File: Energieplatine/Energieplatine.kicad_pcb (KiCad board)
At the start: 2 copper layers, 13 parts, among them J1 USB_C_Receptacle_PowerOnly_6P, J2 Conn_01x02_Pin, U1 4027, U2 TL072, U3 LM2576HVT-ADJ

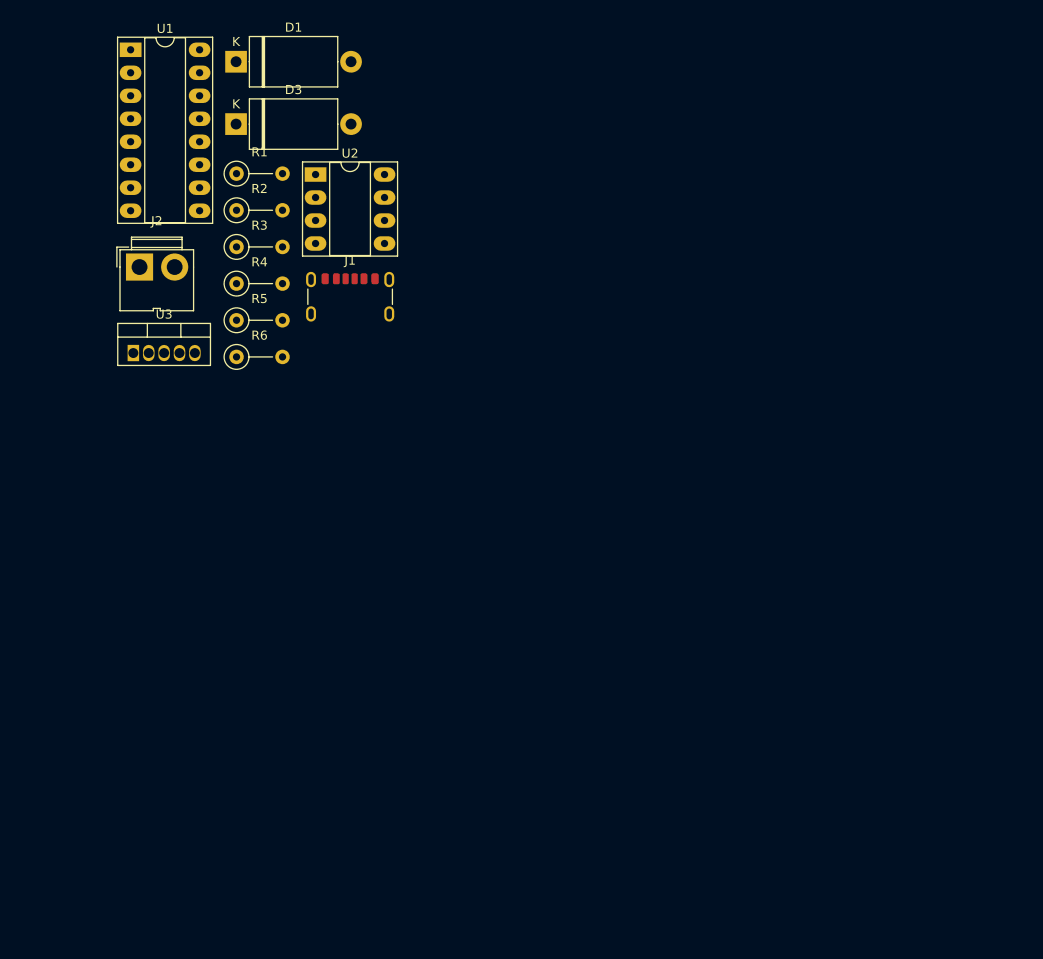
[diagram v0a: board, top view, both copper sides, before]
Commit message: Layout is has no DRC errors.
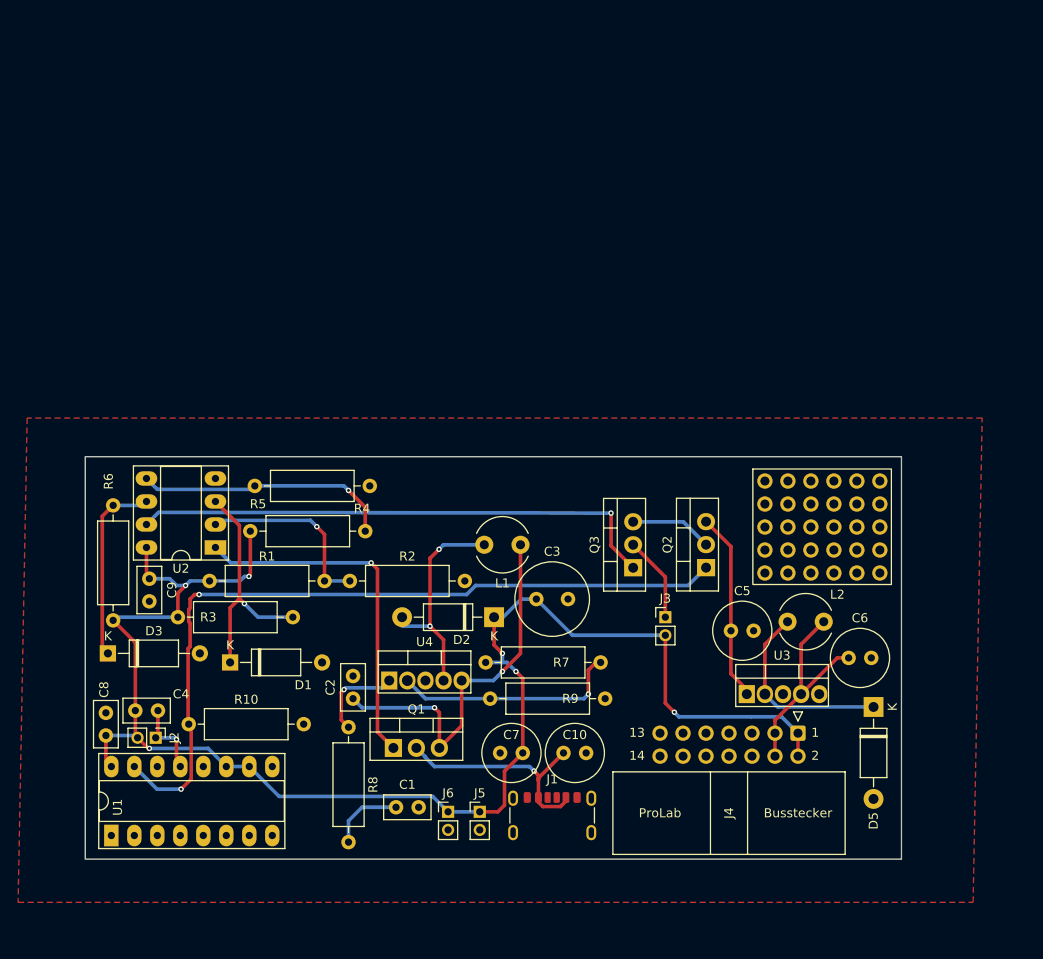
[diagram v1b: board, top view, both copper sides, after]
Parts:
- added C1: 330n, Capacitor_THT:C_Disc_D5.0mm_W2.5mm_P2.50mm, F.Cu at (128.8, 149.5)
- added C10: 100u, Capacitor_THT:C_Radial_D6.3mm_H11.0mm_P2.50mm, F.Cu at (147.2, 143.5)
- added C2: 100n, Capacitor_THT:C_Disc_D5.0mm_W2.5mm_P2.50mm, F.Cu at (124.0, 137.5)
- added C3: 470u, Capacitor_THT:C_Radial_D8.0mm_H11.5mm_P3.50mm, F.Cu at (144.2, 126.5)
- added C4: 100n, Capacitor_THT:C_Disc_D5.0mm_W2.5mm_P2.50mm, F.Cu at (102.5, 138.8)
- added C5: 100u, Capacitor_THT:C_Radial_D6.3mm_H11.0mm_P2.50mm, F.Cu at (165.8, 130.0)
- added C6: 100u, Capacitor_THT:C_Radial_D6.3mm_H11.0mm_P2.50mm, F.Cu at (178.8, 133.0)
- added C7: 100u, Capacitor_THT:C_Radial_D6.3mm_H11.0mm_P2.50mm, F.Cu at (140.2, 143.5)
- added C8: 100n, Capacitor_THT:C_Disc_D5.0mm_W2.5mm_P2.50mm, F.Cu at (96.7, 141.6)
- added C9: 100n, Capacitor_THT:C_Disc_D5.0mm_W2.5mm_P2.50mm, F.Cu at (101.5, 124.2)
- added D2: 1N5817, Diode_THT:D_DO-41_SOD81_P10.16mm_Horizontal, F.Cu at (139.6, 128.5)
- added D5: 1N5822, Diode_THT:D_DO-41_SOD81_P10.16mm_Horizontal, F.Cu at (181.5, 138.4)
- added J3: Conn_01x02_Pin, Connector_PinHeader_2.00mm:PinHeader_1x02_P2.00mm_Vertical, F.Cu at (158.5, 128.5)
- added J4: Conn_02x07_Odd_Even, Projektlabor:Prolab_Busstecker, F.Cu at (165.5, 142.5)
- added J5: Conn_01x02_Pin, Connector_PinHeader_2.00mm:PinHeader_1x02_P2.00mm_Vertical, F.Cu at (138.0, 150.0)
- added J6: Conn_01x02_Pin, Connector_PinHeader_2.00mm:PinHeader_1x02_P2.00mm_Vertical, F.Cu at (134.5, 150.0)
- added L1: 100u, Inductor_THT:L_Radial_D6.0mm_P4.00mm, F.Cu at (142.5, 120.5)
- added L2: 100u, Inductor_THT:L_Radial_D6.0mm_P4.00mm, F.Cu at (172.0, 129.0)
- added Q1: IRF9540N, Package_TO_SOT_THT:TO-220-3_Vertical, F.Cu at (128.5, 142.9)
- added Q2: IRF9540N, Package_TO_SOT_THT:TO-220-3_Vertical, F.Cu at (163.0, 123.0)
- added Q3: IRF540N, Package_TO_SOT_THT:TO-220-3_Vertical, F.Cu at (154.9, 123.0)
- added R10: 1k, Resistor_THT:R_Axial_DIN0309_L9.0mm_D3.2mm_P12.70mm_Horizontal, F.Cu at (105.8, 140.3)
- added R7: 410k, Resistor_THT:R_Axial_DIN0309_L9.0mm_D3.2mm_P12.70mm_Horizontal, F.Cu at (138.7, 133.5)
- added R8: 2.2k, Resistor_THT:R_Axial_DIN0309_L9.0mm_D3.2mm_P12.70mm_Horizontal, F.Cu at (123.5, 140.7)
- added R9: 41k, Resistor_THT:R_Axial_DIN0309_L9.0mm_D3.2mm_P12.70mm_Horizontal, F.Cu at (139.2, 137.5)
- added REF**: Panikraster_05x05, Panikraster_v2:Panikraster_05x05, F.Cu at (169.5, 113.5)
- added U4: LM2577T-ADJ, Projektlabor:TO-220-5_Vertical_Brolab, F.Cu at (128.5, 135.5)
- D1, D3: footprint Diode_THT:D_DO-27_P12.70mm_Horizontal -> Diode_THT:D_A-405_P10.16mm_Horizontal
- J2: footprint Connector:JWT_A3963_1x02_P3.96mm_Vertical -> Connector_PinHeader_2.00mm:PinHeader_1x02_P2.00mm_Vertical
- R1, R2, R3, R4, R5, R6: footprint Resistor_THT:R_Axial_DIN0207_L6.3mm_D2.5mm_P5.08mm_Vertical -> Resistor_THT:R_Axial_DIN0309_L9.0mm_D3.2mm_P12.70mm_Horizontal
- U3: footprint Package_TO_SOT_THT:TO-220-5_Vertical -> Projektlabor:TO-220-5_Vertical_Brolab
- moved U1 86.8 mm to (97.3, 152.6), turned to 90 degrees
- moved U3 78.0 mm to (168.0, 137.0)
- moved D1 66.4 mm to (110.4, 133.5)
- moved J1 61.5 mm to (146.0, 151.5)
- moved D3 60.2 mm to (96.9, 132.5)
- moved J2 52.0 mm to (102.2, 141.8), turned to -90 degrees
- moved R1 45.1 mm to (108.2, 124.5)
- moved R2 42.8 mm to (123.7, 124.5)
- moved U2 42.7 mm to (108.8, 120.8), turned to 180 degrees
- moved R3 41.4 mm to (104.7, 128.5)
- moved R6 32.1 mm to (97.5, 128.8), turned to 90 degrees
- moved R4 27.4 mm to (112.7, 119.0)
- moved R5 18.4 mm to (113.2, 114.0)
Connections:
- U2 pad 7: unconnected-(U2-Pad7) -> undervoltage_logic
- U3 pad 1: unconnected-(U3-VIN-Pad1) -> Net-(Q2-S)
- U3 pad 2: unconnected-(U3-OUT-Pad2) -> Net-(D5-K)
- U3 pad 3: unconnected-(U3-GND-Pad3) -> GND
- U3 pad 4: unconnected-(U3-FB-Pad4) -> Power_5V
- U3 pad 5: unconnected-(U3-~{ON}/OFF-Pad5) -> GND
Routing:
- net Bat+_12V: track 0.00 -> 169.6 mm, vias 0 -> 6
- net FF_out: track 0.00 -> 86.5 mm, vias 0 -> 2
- net undervoltage_logic: track 0.00 -> 59.0 mm, vias 0 -> 1
- net Net-(Q1-S): track 0.00 -> 42.3 mm, vias 0 -> 2
- net overvoltage_logic: track 0.00 -> 39.4 mm, vias 0 -> 1
- net Net-(U2B-+): track 0.00 -> 28.4 mm, vias 0 -> 1
- net USB_5V: track 0.00 -> 26.1 mm, vias 0 -> 1
- net Net-(U4-OUT): track 0.00 -> 25.2 mm, vias 0 -> 1
- net Net-(D1-K): track 0.00 -> 25.1 mm, vias 0 -> 1
- net Power_5V: track 0.00 -> 24.0 mm
- net Net-(D2-A): track 0.00 -> 23.9 mm, vias 0 -> 2
- net Net-(D5-K): track 0.00 -> 21.9 mm
- net Net-(D3-K): track 0.00 -> 21.0 mm
- net Net-(Q2-S): track 0.00 -> 20.9 mm
- net Net-(U2A--): track 0.00 -> 20.8 mm, vias 0 -> 1
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- added copper zone on F.Cu, net GND
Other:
- board outline added: 90.2 x 44.4 mm

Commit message: PCB updated
Footprints der Widerstände angepasst, daraufhin Layout der Platine angepasst.
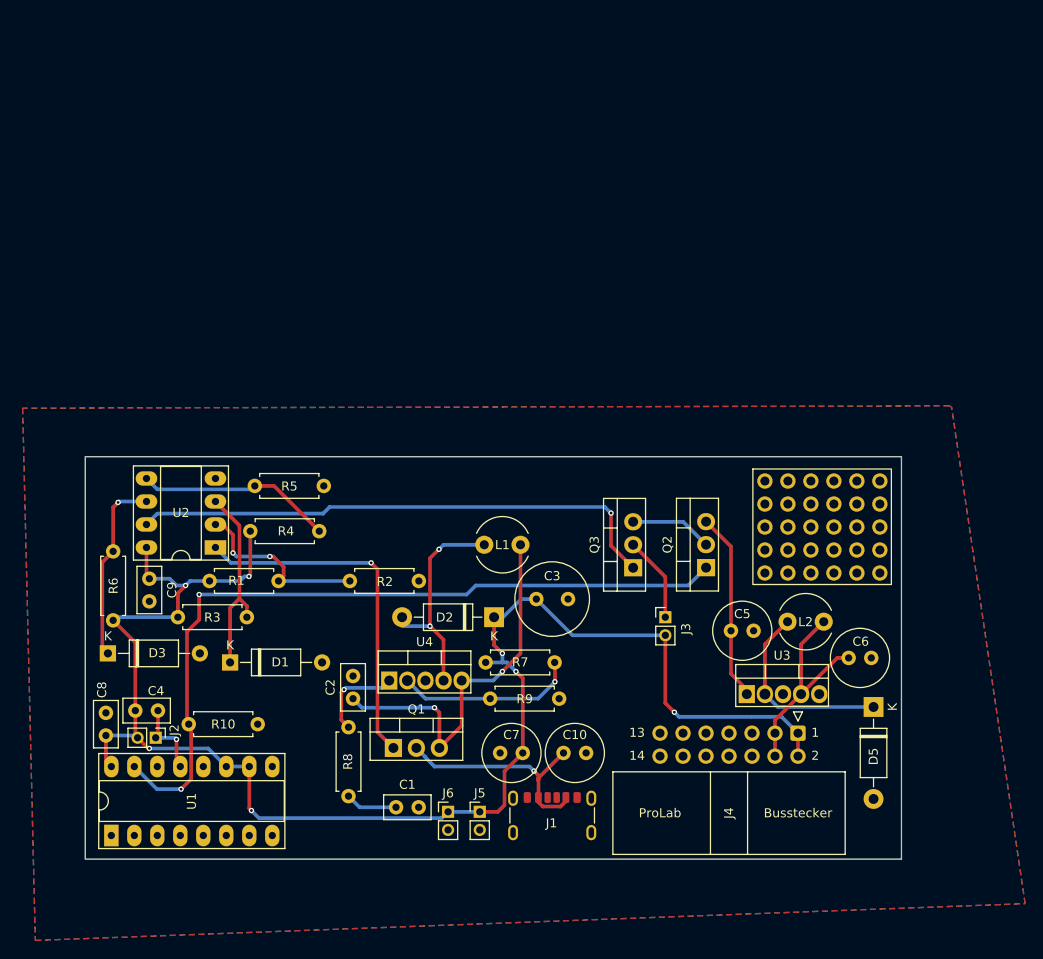
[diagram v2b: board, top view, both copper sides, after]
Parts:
- R1, R10, R2, R3, R4, R5, R6, R7, R8, R9: footprint Resistor_THT:R_Axial_DIN0309_L9.0mm_D3.2mm_P12.70mm_Horizontal -> Resistor_THT:R_Axial_DIN0207_L6.3mm_D2.5mm_P7.62mm_Horizontal
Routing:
- net Net-(U2B-+): track 28.4 -> 21.7 mm, vias 1 -> 0
- net Net-(U4-OUT): track 25.2 -> 20.3 mm
- net Net-(D1-K): track 25.1 -> 20.7 mm, vias 1 -> 0
- net Bat+_12V: track 169.6 -> 172.8 mm, vias 6 -> 7
- net Net-(C1-Pad1): track 8.22 -> 5.76 mm
- net Net-(U2A--): track 20.8 -> 20.3 mm, vias 1 -> 2
- net Net-(D3-K): track 21.0 -> 21.4 mm, vias 0 -> 1
- added copper zone on B.Cu, net GND

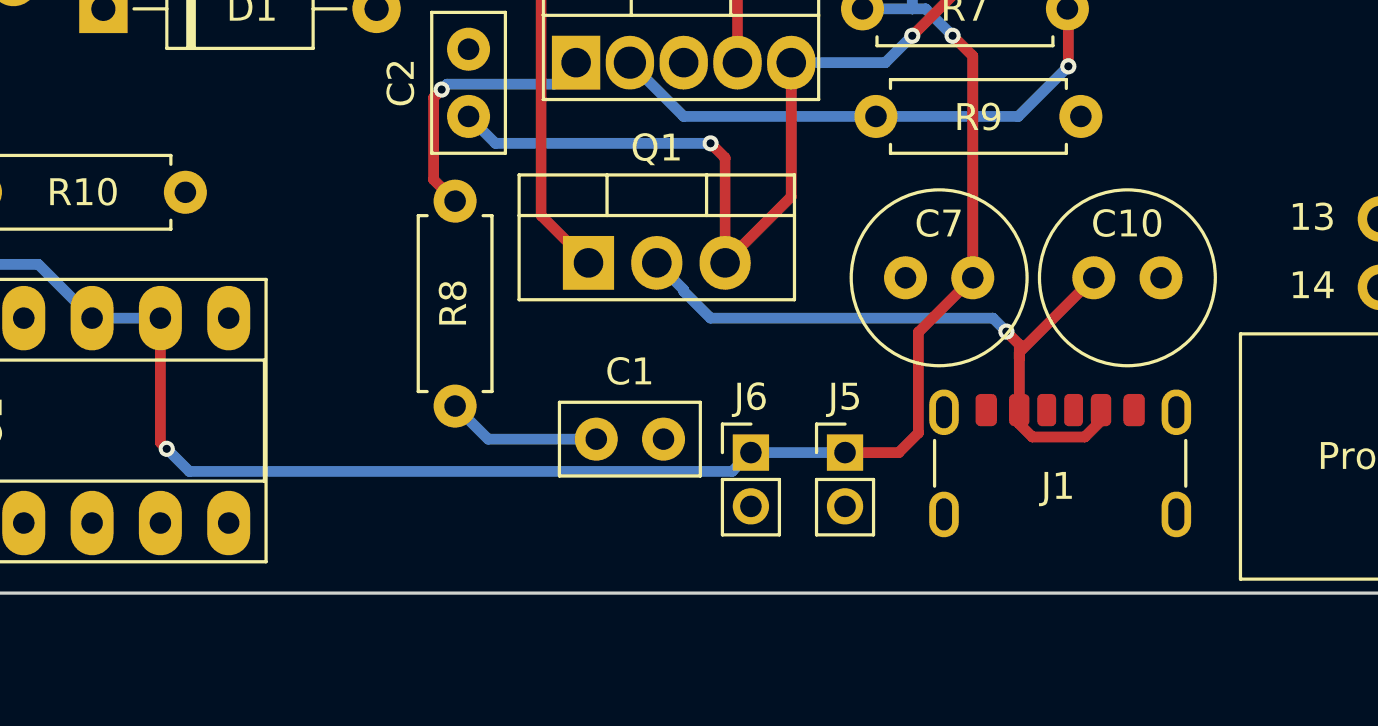
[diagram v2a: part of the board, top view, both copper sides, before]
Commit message: added usb-typeA
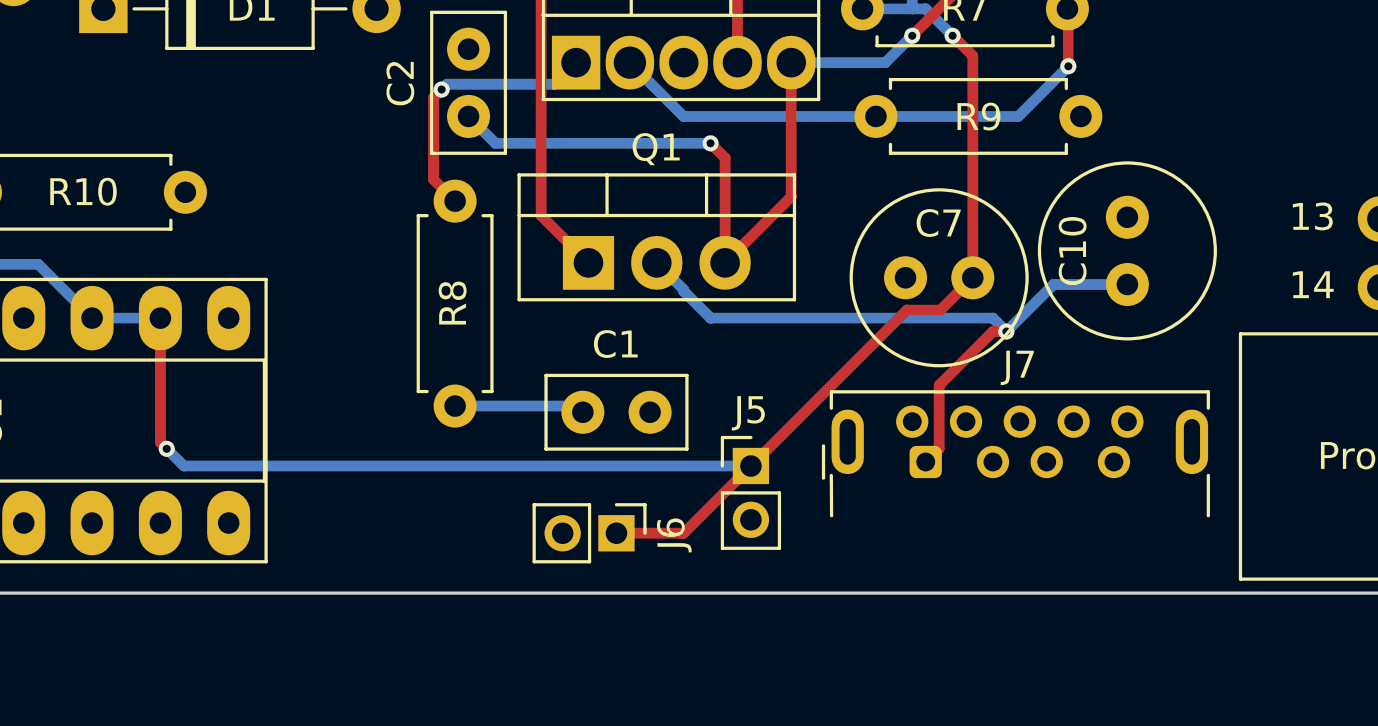
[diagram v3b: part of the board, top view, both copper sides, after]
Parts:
- removed J1: USB_C_Receptacle_PowerOnly_6P, Connector_USB:USB_C_Receptacle_GCT_USB4125-xx-x-0190_6P_TopMnt_Horizontal
- added J7: USB3_A, Projektlabor:USB3_A_Molex_48393-001_short, F.Cu at (141.0, 150.3)
- moved J6 5.83 mm to (129.5, 153.0), turned to -90 degrees
- moved J5 3.54 mm to (134.5, 150.5)
- moved C10 1.27 mm to (148.5, 143.8), turned to 90 degrees
- moved C1 1.12 mm to (128.2, 148.5)
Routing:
- net Bat+_12V: track 172.8 -> 176.5 mm
- net Net-(C1-Pad1): track 5.76 -> 4.85 mm
